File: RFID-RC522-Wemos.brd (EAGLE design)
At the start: 99.8 x 80.5 mm, 18 parts, among them CON1 LCD, J4 VIN

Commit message: added missing values
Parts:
- BOARD1: value (none) -> 8x10
- C1: device SPCoast:E5-10.5 -> SPCoast:0810-CAP
- LED1, LED3: value (none) -> G
- LED2, LED4: value (none) -> R
- R1, R2: value (none) -> 1K0
- U$1: value (none) -> mini
- U$3: value (none) -> LCD
- VR: value (none) -> 5v
- moved C1 1.80 mm to (14.0, 73.7), turned to 180 degrees
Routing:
- net +9V: track 68.6 -> 66.4 mm
- net VCC: track 122.2 -> 121.5 mm

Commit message: added missing values
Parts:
- C2: value .1uF -> 1uF
- C3: value .1uF -> 10uF
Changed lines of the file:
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@@
 <elements>
 <element name="C1" library="SPCoast" package="0810-CAP" value="220uF" x="13.97" y="73.66" rot="R180"/>
-<element name="C2" library="SPCoast" package="0805-CAP" value=".1uF" x="5.08" y="24.13" rot="R180"/>
-<element name="C3" library="SPCoast" package="0805-CAP" value=".1uF" x="5.08" y="17.78" rot="R180"/>
+<element name="C2" library="SPCoast" package="0805-CAP" value="1uF" x="5.08" y="24.13" rot="R180"/>
+<element name="C3" library="SPCoast" package="0805-CAP" value="10uF" x="5.08" y="17.78" rot="R180"/>
 <element name="CON1" library="SPCoast" package="I2C-L" value="LCD" x="19.05" y="53.34" smashed="yes">
 <attribute name="NAME" x="11.938" y="39.624" size="0.889" layer="25" font="vector" ratio="11" rot="R90"/>
@@
 <contactref element="CON1" pad="V+"/>
 <contactref element="CON1" pad="V+@1"/>
-<wire x1="8.255" y1="17.78" x2="5.98" y2="17.78" width="0.8128" layer="1"/>
+<wire x1="8.255" y1="17.78" x2="5.98" y2="17.78" width="0.4064" layer="1"/>
 <wire x1="18.923" y1="45.705" x2="18.938" y2="45.72" width="0.6096" layer="16"/>
 <wire x1="18.938" y1="45.72" x2="20.32" y2="45.72" width="0.8128" layer="16"/>

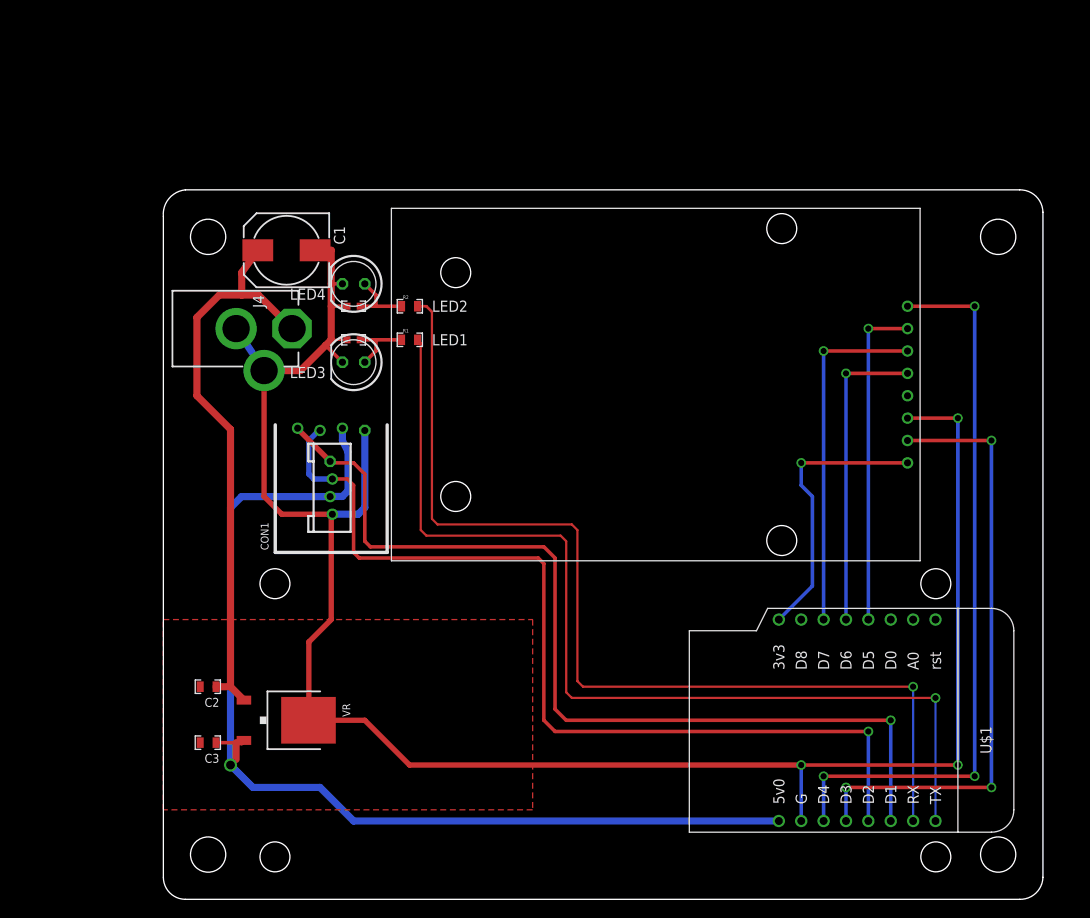
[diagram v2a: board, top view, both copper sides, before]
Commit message: normalized values
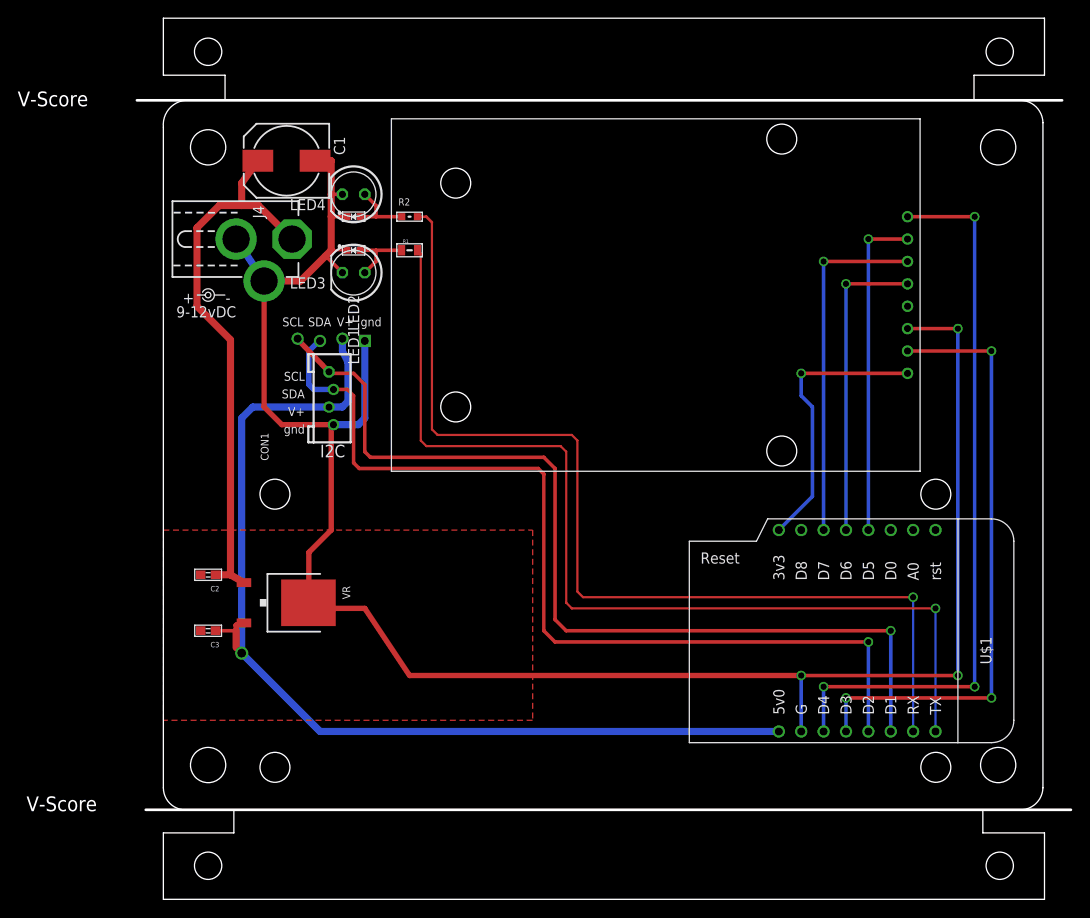
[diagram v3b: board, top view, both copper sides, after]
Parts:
- C2, C3: device SPCoast:0805-CAP -> SPCoast:0603-CAP
- J4: value VIN -> 2.1mm
- LOGO1: value DOC-OSHW-LOGOL -> OSHW
- POWER: device SPCoast:POWER_USAGE -> SPCoast:PWR_LABEL
- R2: device SPCoast:0805-RES -> SPCoast:0603-RES
- U$1: value mini -> Mini-R2
- VR: value 5v -> CJ7805; device SPCoast:TO252 -> SPCoast:TO-252
- moved VR 13.3 mm to (14.0, 33.7), turned to 0 degrees
- moved C2 12.7 mm to (5.08, 36.8)
- moved C3 12.7 mm to (5.08, 30.5)
- moved J4 10.2 mm to (11.4, 74.9)
- moved LED4 10.2 mm to (21.6, 80.0), turned to 0 degrees
- moved LED3 10.2 mm to (21.6, 71.1), turned to 0 degrees
- moved U$1 10.2 mm to (77.5, 30.5)
- moved U$3 10.2 mm to (50.2, 30.5)
- moved C1 10.2 mm to (14.0, 83.8)
- moved CON1 10.2 mm to (19.1, 63.5)
- moved LED1 10.2 mm to (21.6, 73.7), turned to 0 degrees
- moved LED2 10.2 mm to (21.6, 77.5), turned to 0 degrees
- moved LOGO1 10.2 mm to (50.8, 68.6)
- moved POWER 10.2 mm to (5.08, 68.6)
- moved R1 10.2 mm to (27.9, 73.7)
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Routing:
- net VCC: track 121.5 -> 118.1 mm
- net +9V: track 66.4 -> 63.5 mm
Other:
- board size 99.8 x 80.5 mm -> 106 x 100 mm
